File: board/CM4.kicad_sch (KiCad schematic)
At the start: 4 parts, among them J201 DF40C-100DS-0.4V(51), J202 DF40C-100DS-0.4V(51)

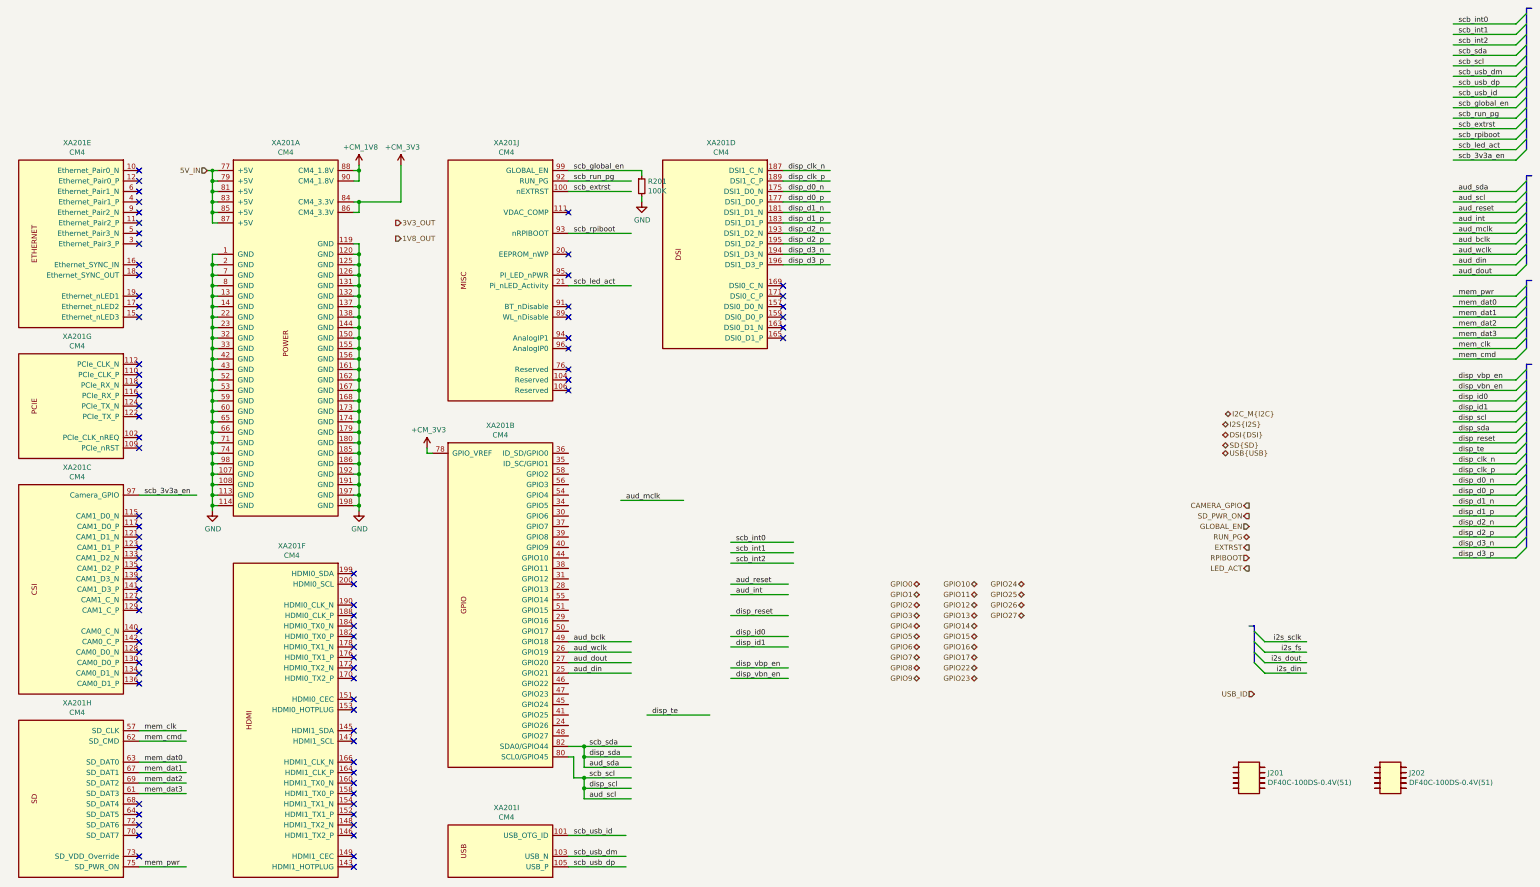
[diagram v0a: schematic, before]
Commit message: Added testpoints and other fixes
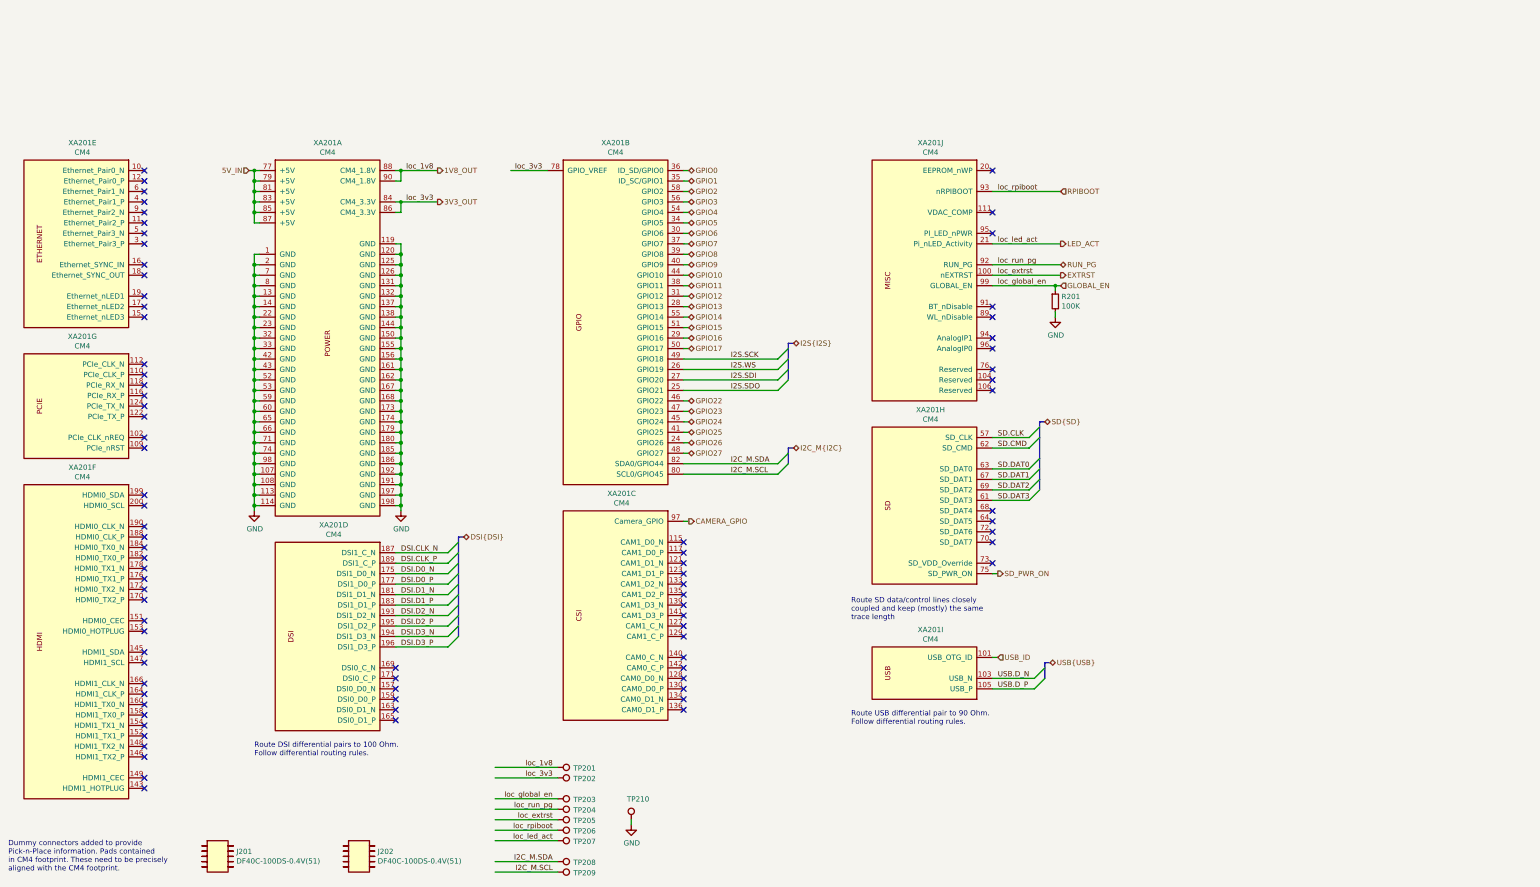
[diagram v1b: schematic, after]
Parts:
- added TP201, TP202, TP203, TP204, TP205, TP206, TP207, TP208, TP209, TP210: TestPoint, DIYPie:TestPoint_Pad_D1.5mm, symbol DIYPie:TestPoint
- J201: renamed from J202; footprint DIYPie:HIROSE_DF40C-100DS-0.4V(51)_NoPads -> DIYPie:hirose_DF40C-100DS-0.4V(51)_NoPads
- J202: renamed from J201; footprint DIYPie:HIROSE_DF40C-100DS-0.4V(51)_NoPads -> DIYPie:hirose_DF40C-100DS-0.4V(51)_NoPads
- XA201: footprint DIYPie:CM4_LOW_PROFILE_NoHoles -> DIYPie:CM4_LowProfile_NoHoles
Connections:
- net +1V8 is gone; now on net 1V8_OUT: XA201.88 (CM4_1.8V), XA201.90 (CM4_1.8V)
- net +3V3 is gone; now on net 3V3_OUT: XA201.78 (GPIO_VREF), XA201.84 (CM4_3.3V), XA201.86 (CM4_3.3V)
- net mem_pwr is gone; now on net SD_PWR_ON: XA201.75 (SD_PWR_ON)
- net scb_3v3a_en is gone; now on net CAMERA_GPIO: XA201.97 (Camera_GPIO)
- net scb_extrst is gone; now on net EXTRST: XA201.100 (nEXTRST)
- net scb_global_en is gone; now on net GLOBAL_EN: R201.1, XA201.99 (GLOBAL_EN)
- net scb_led_act is gone; now on net LED_ACT: XA201.21 (Pi_nLED_Activity)
- net scb_rpiboot is gone; now on net RPIBOOT: XA201.93 (nRPIBOOT)
- net scb_run_pg is gone; now on net RUN_PG: XA201.92 (RUN_PG)
- net scb_usb_id is gone; now on net USB_ID: XA201.101 (USB_OTG_ID)
- net 1V8_OUT: now also TP201.1
- net 3V3_OUT: now also TP202.1
- net EXTRST: now also TP205.1
- net GLOBAL_EN: now also TP203.1
- net GND: now also TP210.1
- net GPIO0: now also XA201.36 (ID_SD/GPIO0)
- net GPIO1: now also XA201.35 (ID_SC/GPIO1)
- net GPIO10: now also XA201.44 (GPIO10)
- net GPIO11: now also XA201.38 (GPIO11)
- net GPIO12: now also XA201.31 (GPIO12)
- net GPIO13: now also XA201.28 (GPIO13)
- net GPIO14: now also XA201.55 (GPIO14)
- net GPIO15: now also XA201.51 (GPIO15)
- net GPIO16: now also XA201.29 (GPIO16)
- net GPIO17: now also XA201.50 (GPIO17)
- net GPIO2: now also XA201.58 (GPIO2)
- net GPIO22: now also XA201.46 (GPIO22)
- net GPIO23: now also XA201.47 (GPIO23)
- net GPIO24: now also XA201.45 (GPIO24)
- net GPIO25: now also XA201.41 (GPIO25)
- net GPIO26: now also XA201.24 (GPIO26)
- net GPIO27: now also XA201.48 (GPIO27)
- net GPIO3: now also XA201.56 (GPIO3)
- net GPIO4: now also XA201.54 (GPIO4)
- net GPIO5: now also XA201.34 (GPIO5)
- net GPIO6: now also XA201.30 (GPIO6)
- net GPIO7: now also XA201.37 (GPIO7)
- net GPIO8: now also XA201.39 (GPIO8)
- net GPIO9: now also XA201.40 (GPIO9)
- net LED_ACT: now also TP207.1
- net RPIBOOT: now also TP206.1
- net RUN_PG: now also TP204.1
- net aud_bclk renamed I2S.SCK
- net aud_din renamed I2S.SDO
- net aud_dout renamed I2S.SDI
- net aud_scl renamed I2C_M.SCL
- net I2C_M.SCL: now also TP209.1
- net aud_sda renamed I2C_M.SDA
- net I2C_M.SDA: now also TP208.1
- net aud_wclk renamed I2S.WS
- net disp_clk_n renamed DSI.CLK_N
- net disp_clk_p renamed DSI.CLK_P
- net disp_d0_n renamed DSI.D0_N
- net disp_d0_p renamed DSI.D0_P
- net disp_d1_n renamed DSI.D1_N
- net disp_d1_p renamed DSI.D1_P
- net disp_d2_n renamed DSI.D2_N
- net disp_d2_p renamed DSI.D2_P
- net disp_d3_n renamed DSI.D3_N
- net disp_d3_p renamed DSI.D3_P
- net mem_clk renamed SD.CLK
- net mem_cmd renamed SD.CMD
- net mem_dat0 renamed SD.DAT0
- net mem_dat1 renamed SD.DAT1
- net mem_dat2 renamed SD.DAT2
- net mem_dat3 renamed SD.DAT3
- net scb_usb_dm renamed USB.D_N
- net scb_usb_dp renamed USB.D_P
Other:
- note added: "Dummy connectors added to provide Pick-n-Place information. Pads contained in CM4 footprint. These need to be precisely aligned with the CM4 footprint."
- note added: "Route DSI differential pairs to 100 Ohm. Follow differential routing rules."
- note added: "Route SD data/control lines closely coupled and keep (mostly) the same trace length"
- note added: "Route USB differential pair to 90 Ohm. Follow differential routing rules."
- title: (none) -> asd
- moved on the sheet: J201, J202, R201, XA201A, XA201B, XA201C, XA201D, XA201E, XA201F, XA201G, XA201H, XA201I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
